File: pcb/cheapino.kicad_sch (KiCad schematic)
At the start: 50 parts, among them K1 SW_Push, K10 SW_Push, K11 SW_Push, K12 SW_Push, K13 SW_Push, K14 SW_Push, K15 SW_Push, K16 SW_Push, K17 SW_Push, K18 SW_Push, K2 SW_Push, K3 SW_Push, K4 SW_Push, K5 SW_Push, K6 SW_Push, K7 SW_Push, K8 SW_Push, K9 SW_Push, U1 RP2040-Zero

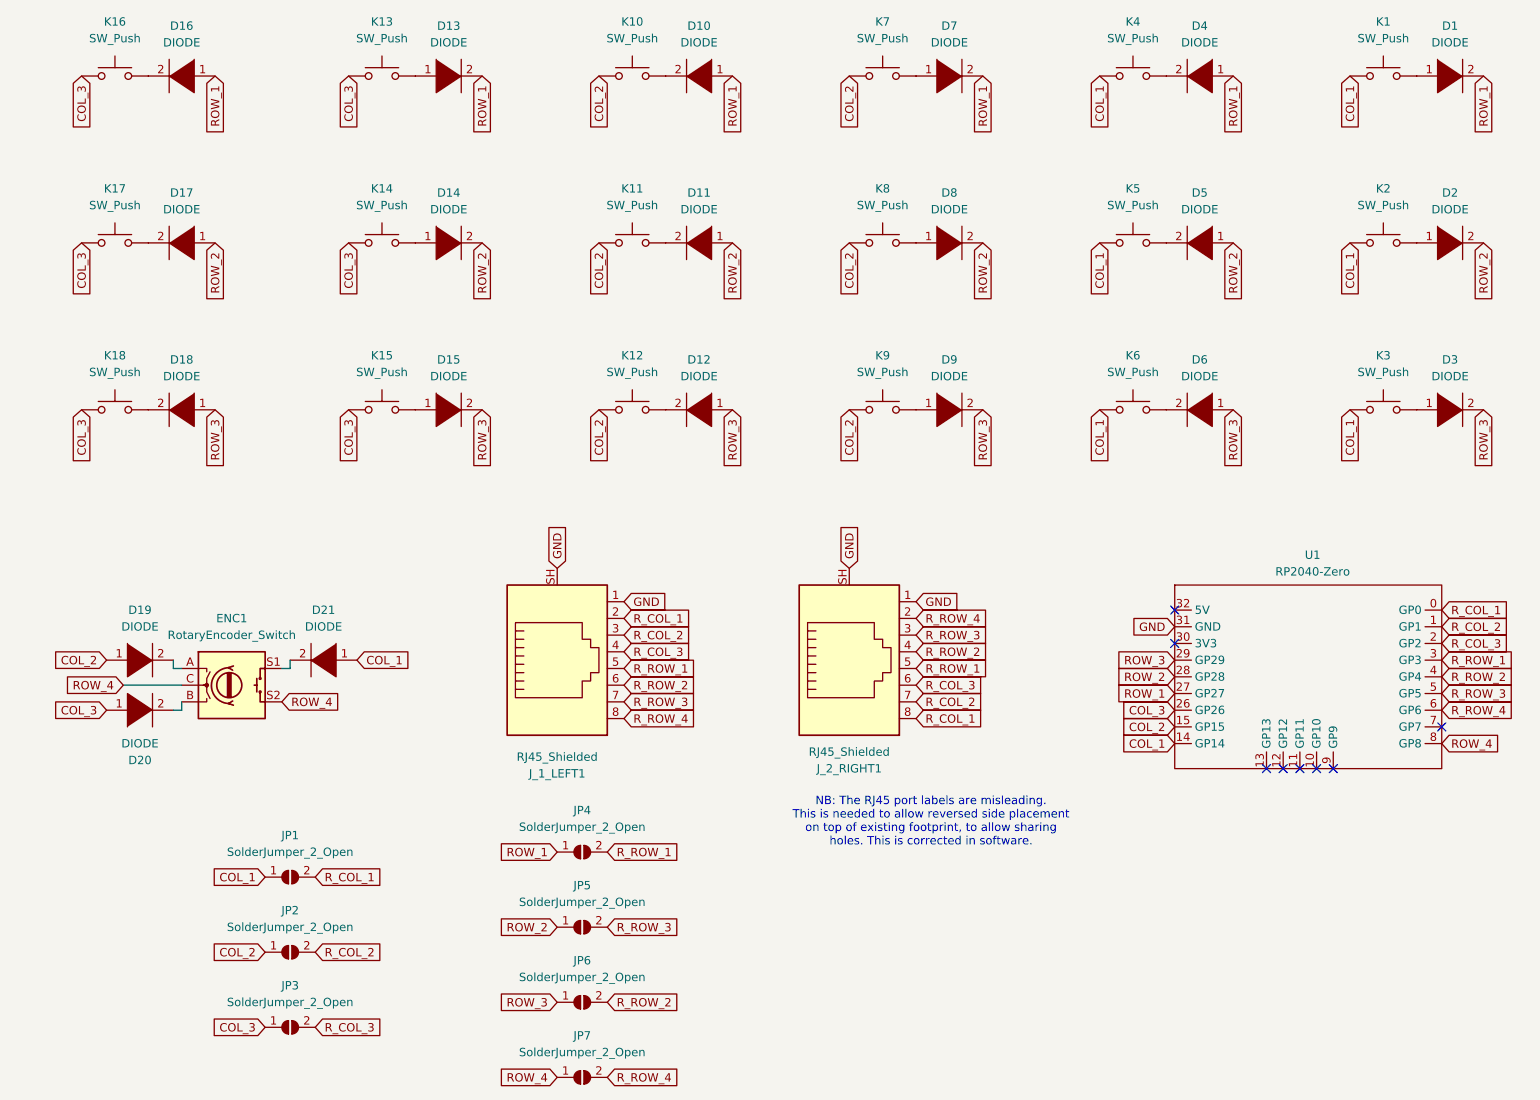
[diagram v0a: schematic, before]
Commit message: First pass, schematic updated for bare RP2040, SK6812-Mini RGB LED with proper series resistor and logic level shifter.
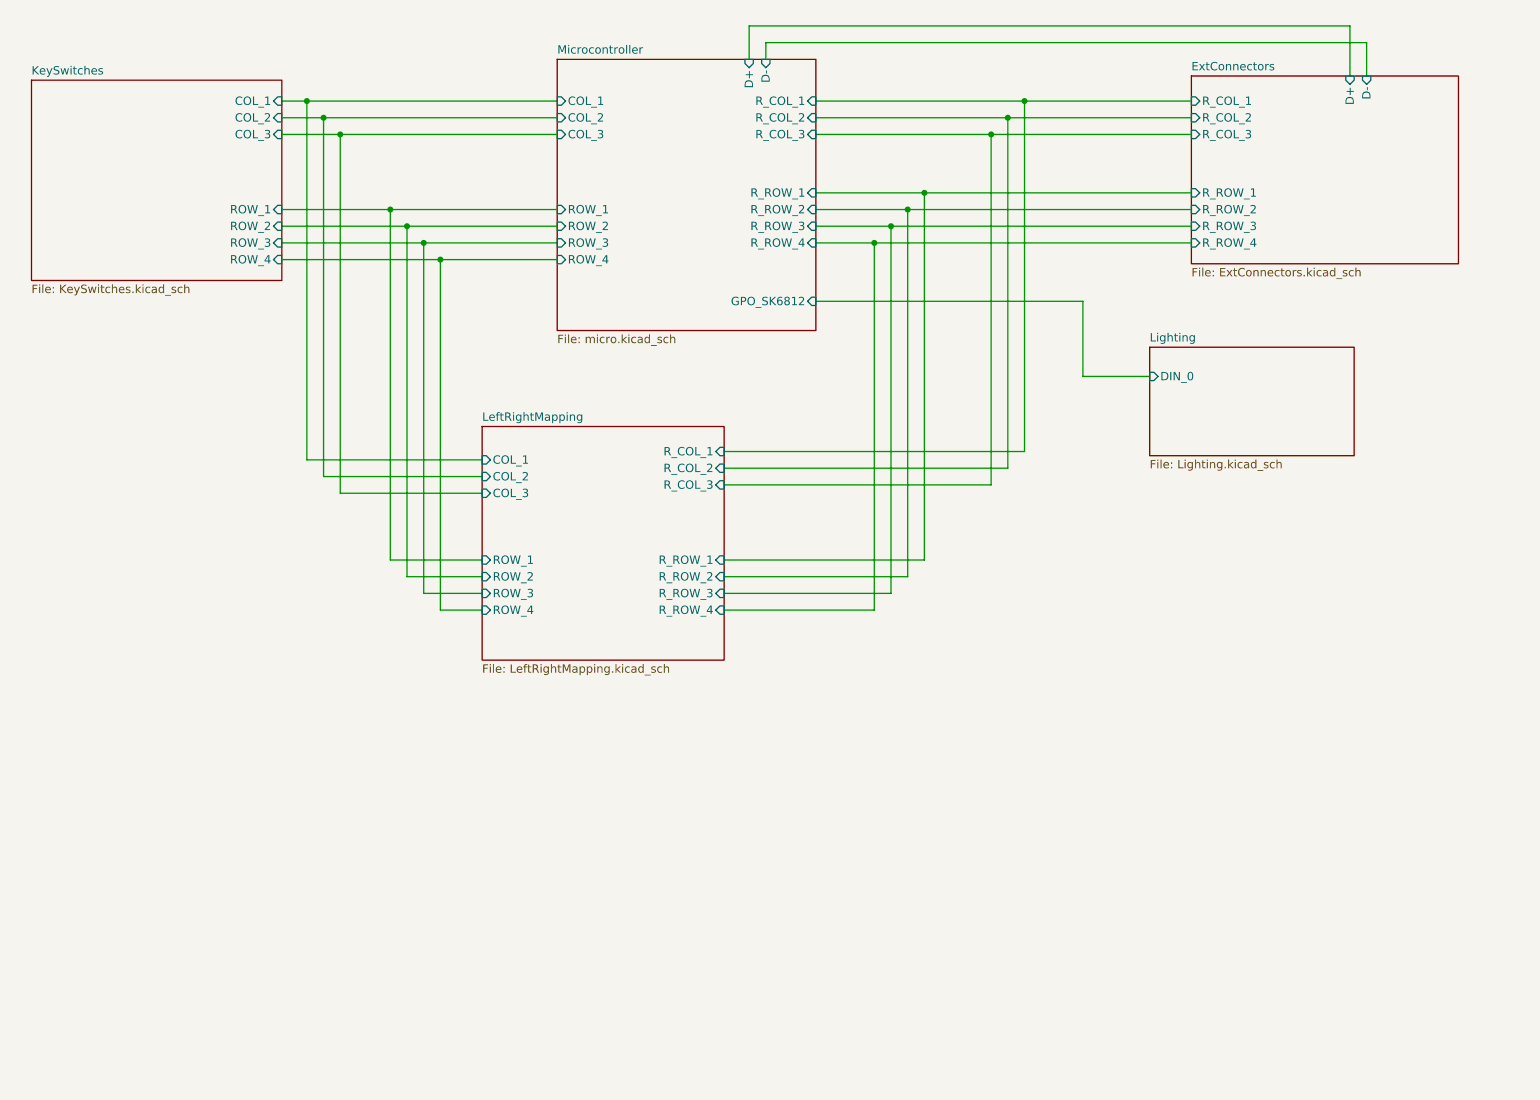
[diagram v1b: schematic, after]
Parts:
- removed D1, D10, D11, D12, D13, D14, D15, D17, D18, D19, D2, D20, D21, D3, D4, D5, D6, D7, D8, D9: DIODE, keebio:Diode-dual, symbol pspice:DIODE
- removed D16: DIODE, keyboard_parts:D_SOD123_axial, symbol pspice:DIODE
- removed ENC1: RotaryEncoder_Switch, Rotary_Encoder:RotaryEncoder_Alps_EC11E-Switch_Vertical_H20mm, symbol Device:RotaryEncoder_Switch
- removed JP1, JP2, JP3, JP4, JP5, JP6, JP7: SolderJumper_2_Open, Jumper:SolderJumper-2_P1.3mm_Open_TrianglePad1.0x1.5mm, symbol Jumper:SolderJumper_2_Open
- removed J_1_LEFT1, J_2_RIGHT1: RJ45_Shielded, Connector_RJ:RJ45_Ninigi_GE, symbol Connector:RJ45_Shielded
- removed K1, K10, K11, K12, K13, K14, K15, K16, K17, K18, K2, K3, K4, K5, K6, K7, K8, K9: SW_Push, project_footprints:Kailh_socket_MX_optional_reversible, symbol Switch:SW_Push
- removed U1: RP2040-Zero, rp2040:MCU_RP2040_Zero_34, symbol project:RP2040-Zero
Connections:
- no-connect marks 8 -> 0
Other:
- added sheet ExtConnectors (ExtConnectors.kicad_sch)
- added sheet KeySwitches (KeySwitches.kicad_sch)
- added sheet LeftRightMapping (LeftRightMapping.kicad_sch)
- added sheet Lighting (Lighting.kicad_sch)
- added sheet Microcontroller (micro.kicad_sch)
- note removed: "NB: The RJ45 port labels are misleading. This is needed to allow reversed side placement on top of existing footprint, to allow sharing holes. This is corrected in software."

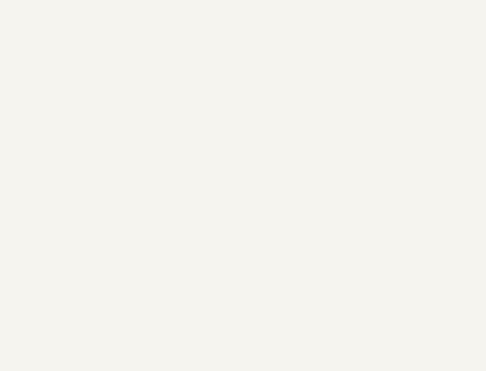
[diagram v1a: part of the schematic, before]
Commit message: First pass of applying footprints to most components.
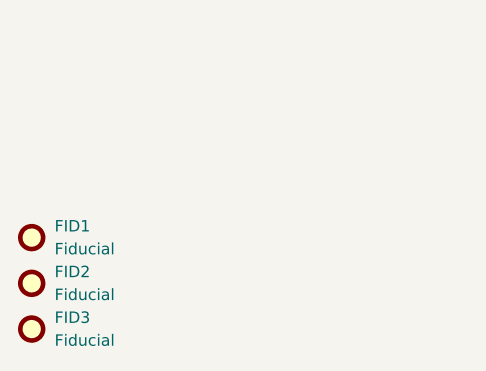
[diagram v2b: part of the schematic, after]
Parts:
- added FID1, FID2, FID3: Fiducial, symbol Mechanical:Fiducial
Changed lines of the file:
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@@
+		)
+	)
+	(symbol
+		(lib_id "Mechanical:Fiducial")
+		(at 31.75 175.26 0)
+		(unit 1)
+		(exclude_from_sim yes)
+		(in_bom no)
+		(on_board yes)
+		(dnp no)
+		(fields_autoplaced yes)
+		(property "Reference" "FID1"
+			(at 34.29 173.9899 0)
+			(effects
+				(font
+					(size 1.27 1.27)
+				)
+				(justify left)
+			)
+		)
+		(property "Value" "Fiducial"
+			(at 34.29 176.5299 0)
+			(effects
+				(font
+					(size 1.27 1.27)
+				)
+				(justify left)
+			)
+		)
+		(property "Footprint" ""
+			(at 31.75 175.26 0)
+			(effects
+				(font
+					(size 1.27 1.27)
+				)
+				(hide yes)
+			)
+		)
+		(property "Datasheet" "~"
+			(at 31.75 175.26 0)
+			(effects
+				(font
+					(size 1.27 1.27)
+				)
+				(hide yes)
+			)
+		)
+		(property "Description" "Fiducial Marker"
+			(at 31.75 175.26 0)
+			(effects
+				(font
+					(size 1.27 1.27)
+				)
+				(hide yes)
+			)
+		)
+		(instances
+			(project ""
+				(path "/9203b006-47ac-4f34-8cc4-2b709e3df56f"
+					(reference "FID1")
+					(unit 1)
+				)
+			)
+		)
+	)
+	(symbol
+		(lib_id "Mechanical:Fiducial")
+		(at 31.75 185.42 0)
+		(unit 1)
+		(exclude_from_sim yes)
+		(in_bom no)
+		(on_board yes)
+		(dnp no)
+		(fields_autoplaced yes)
+		(property "Reference" "FID3"
+			(at 34.29 184.1499 0)
+			(effects
+				(font
+					(size 1.27 1.27)
+				)
+				(justify left)
+			)
+		)
+		(property "Value" "Fiducial"
+			(at 34.29 186.6899 0)
+			(effects
+				(font
+					(size 1.27 1.27)
+				)
+				(justify left)
+			)
+		)
+		(property "Footprint" ""
+			(at 31.75 185.42 0)
+			(effects
+				(font
+					(size 1.27 1.27)
+				)
+				(hide yes)
+			)
+		)
+		(property "Datasheet" "~"
+			(at 31.75 185.42 0)
+			(effects
+				(font
+					(size 1.27 1.27)
+				)
+				(hide yes)
+			)
+		)
+		(property "Description" "Fiducial Marker"
+			(at 31.75 185.42 0)
+			(effects
+				(font
+					(size 1.27 1.27)
+				)
+				(hide yes)
+			)
+		)
+		(instances
+			(project "cheapino"
+				(path "/9203b006-47ac-4f34-8cc4-2b709e3df56f"
+					(reference "FID3")
+					(unit 1)
+				)
+			)
+		)
+	)
+	(symbol
+		(lib_id "Mechanical:Fiducial")
+		(at 31.75 180.34 0)
+		(unit 1)
+		(exclude_from_sim yes)
+		(in_bom no)
+		(on_board yes)
+		(dnp no)
+		(fields_autoplaced yes)
+		(property "Reference" "FID2"
+			(at 34.29 179.0699 0)
+			(effects
+				(font
+					(size 1.27 1.27)
+				)
+				(justify left)
+			)
+		)
+		(property "Value" "Fiducial"
+			(at 34.29 181.6099 0)
+			(effects
+				(font
+					(size 1.27 1.27)
+				)
+				(justify left)
+			)
+		)
+		(property "Footprint" ""
+			(at 31.75 180.34 0)
+			(effects
+				(font
+					(size 1.27 1.27)
+				)
+				(hide yes)
+			)
+		)
+		(property "Datasheet" "~"
+			(at 31.75 180.34 0)
+			(effects
+				(font
+					(size 1.27 1.27)
+				)
+				(hide yes)
+			)
+		)
+		(property "Description" "Fiducial Marker"
+			(at 31.75 180.34 0)
+			(effects
+				(font
+					(size 1.27 1.27)
+				)
+				(hide yes)
+			)
+		)
+		(instances
+			(project "cheapino"
+				(path "/9203b006-47ac-4f34-8cc4-2b709e3df56f"
+					(reference "FID2")
+					(unit 1)
+				)
+			)
 		)
 	)

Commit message: Updated all footprints and libraries to match planned components.
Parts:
- FID1, FID2, FID3: footprint (none) -> Fiducial:Fiducial_1.5mm_Mask3mm
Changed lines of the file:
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@@
 			)
 		)
-		(property "Footprint" ""
+		(property "Footprint" "Fiducial:Fiducial_1.5mm_Mask3mm"
 			(at 31.75 175.26 0)
 			(effects
@@
 			)
 		)
-		(property "Footprint" ""
+		(property "Footprint" "Fiducial:Fiducial_1.5mm_Mask3mm"
 			(at 31.75 185.42 0)
 			(effects
@@
 			)
 		)
-		(property "Footprint" ""
+		(property "Footprint" "Fiducial:Fiducial_1.5mm_Mask3mm"
 			(at 31.75 180.34 0)
 			(effects

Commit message: Removed Rotary Encoder for space/flippability reasons and replaced all the key switch footprints that weren't bound properly to the schematic for some reason.
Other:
- sheet KeySwitches ports: added none; removed ROW_4
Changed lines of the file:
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@@
-	)
-	(junction
-		(at 95.25 68.58)
-		(diameter 0)
-		(color 0 0 0 0)
 	)
 	(junction
@@
 	(wire
 		(pts
-			(xy 95.25 121.92) (xy 95.25 68.58)
-		)
-		(stroke
-			(width 0)
-			(type default)
-		)
-	)
-	(wire
-		(pts
 			(xy 168.91 58.42) (xy 209.55 58.42)
 		)
@@
 	(wire
 		(pts
-			(xy 95.25 68.58) (xy 113.03 68.58)
-		)
-		(stroke
-			(width 0)
-			(type default)
-		)
-	)
-	(wire
-		(pts
 			(xy 161.29 66.04) (xy 161.29 121.92)
 		)
@@
 	(wire
 		(pts
-			(xy 101.6 121.92) (xy 95.25 121.92)
-		)
-		(stroke
-			(width 0)
-			(type default)
-		)
-	)
-	(wire
-		(pts
 			(xy 168.91 58.42) (xy 168.91 114.3)
 		)
@@
 		(pts
 			(xy 101.6 101.6) (xy 77.47 101.6)
-		)
-		(stroke
-			(width 0)
-			(type default)
-		)
-	)
-	(wire
-		(pts
-			(xy 71.12 68.58) (xy 95.25 68.58)
 		)
 		(stroke
@@
 			(effects
 				(font
-					(size 1.27 1.27)
-				)
-				(justify right)
-			)
-		)
-		(pin "ROW_4" input
-			(at 71.12 68.58 0)
-			(effects
-				(font

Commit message: Starting to position components and flipping passives as needed. Looking like board size is likely to need to be expanded.
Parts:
- FID1, FID2, FID3: footprint Fiducial:Fiducial_1.5mm_Mask3mm -> Fiducial:Fiducial_1mm_Mask2mm
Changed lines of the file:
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@@
 			)
 		)
-		(property "Footprint" "Fiducial:Fiducial_1.5mm_Mask3mm"
+		(property "Footprint" "Fiducial:Fiducial_1mm_Mask2mm"
 			(at 31.75 175.26 0)
 			(effects
@@
 			)
 		)
-		(property "Footprint" "Fiducial:Fiducial_1.5mm_Mask3mm"
+		(property "Footprint" "Fiducial:Fiducial_1mm_Mask2mm"
 			(at 31.75 185.42 0)
 			(effects
@@
 			)
 		)
-		(property "Footprint" "Fiducial:Fiducial_1.5mm_Mask3mm"
+		(property "Footprint" "Fiducial:Fiducial_1mm_Mask2mm"
 			(at 31.75 180.34 0)
 			(effects
